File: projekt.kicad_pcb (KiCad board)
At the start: 4 copper layers, 65 x 65 mm, 118 parts, among them IC1 DW01+G, IC4 MIC5504-3.3YM5-TR, J1 10118194-0001LF, J10 Conn_01x06_Pin, J2 TP4056, J4 Conn_01x02_Socket, Q1 AO3420, Q2 AO3420, Q3 AO3420, Q4 AO3420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

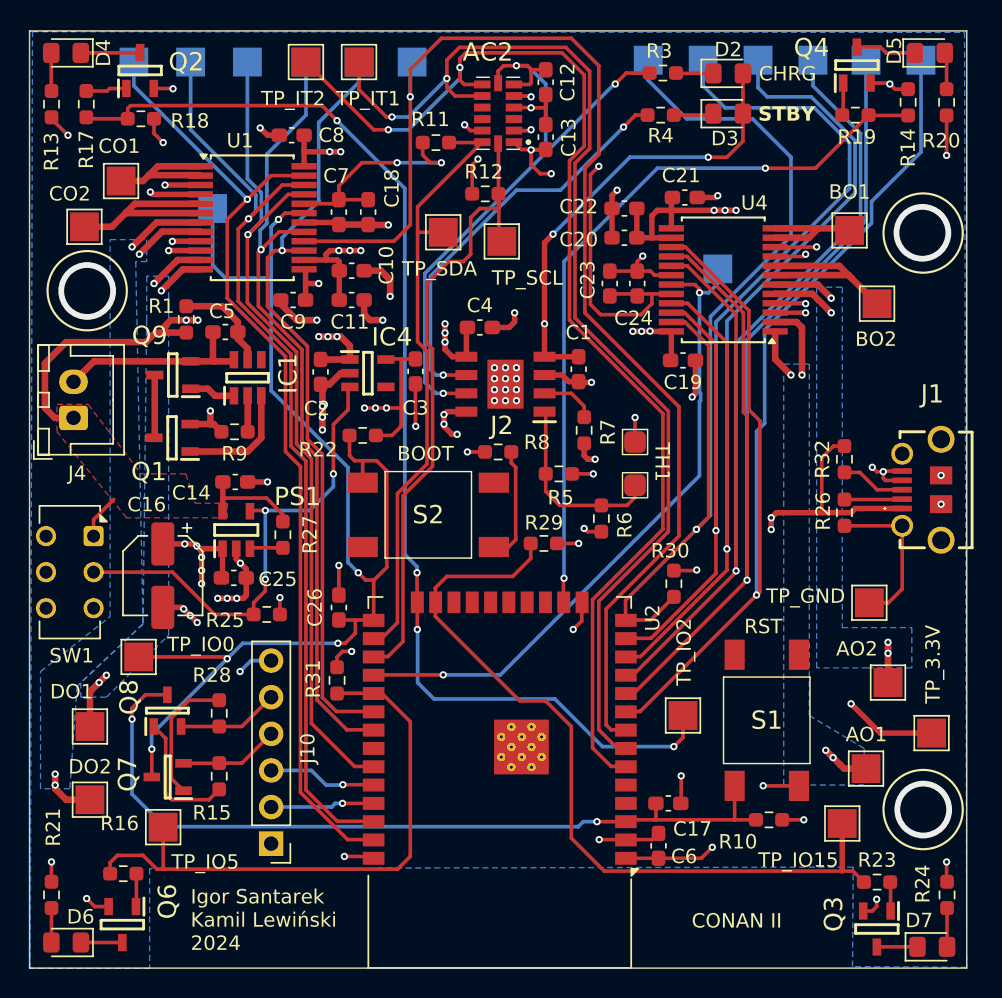
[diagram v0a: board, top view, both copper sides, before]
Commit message: Podmiana esp32 i footprinta switcha
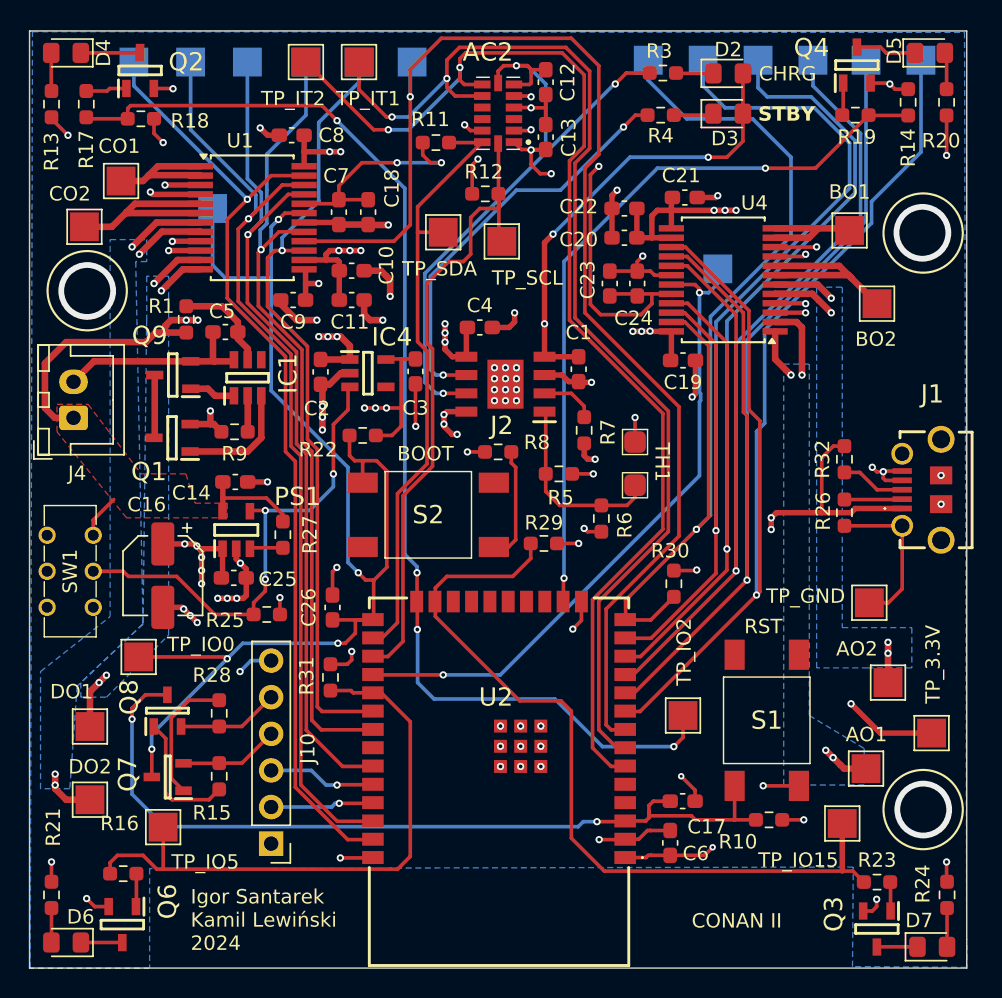
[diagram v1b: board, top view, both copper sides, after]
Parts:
- SW1: footprint Button_Switch_THT:SW_CK_JS202011AQN_DPDT_Angled -> Button_Switch_THT:SS22T20
- U2: value ESP32-WROOM-32E -> ESP32-WROOM-32E-N16; footprint RF_Module:ESP32-WROOM-32D -> SamacSys_Parts:ESP32WROOM32EN16
- moved SW1 2.93 mm to (119.0, 102.4), turned to 90 degrees
- moved U2 2.69 mm to (148.8, 116.7)
- moved C17 1.00 mm to (161.5, 118.3)
- moved C6 0.83 mm to (160.6, 121.2)
- moved R31 0.50 mm to (137.1, 109.7)
- moved C26 0.44 mm to (137.2, 104.9)
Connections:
- SW1 pad 1: /LIPO+ -> unconnected-(SW1-A-Pad1)
- SW1 pad 2: /SW+ -> unconnected-(SW1-B-Pad2)
- SW1 pad 5: unconnected-(SW1-B-Pad5) -> /SW+
- SW1 pad 6: unconnected-(SW1-C-Pad6) -> /LIPO+
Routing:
- net /EN: track 56.9 -> 58.8 mm
- net /BOOT: track 85.1 -> 86.7 mm
- net +3.3V: track 84.6 -> 85.8 mm
- net /DIN1: track 55.6 -> 56.7 mm
- net /LED3: track 55.7 -> 56.3 mm
- net /PWMD: track 54.1 -> 54.6 mm
- net GND: track 138.1 -> 138.6 mm, vias 73 -> 82

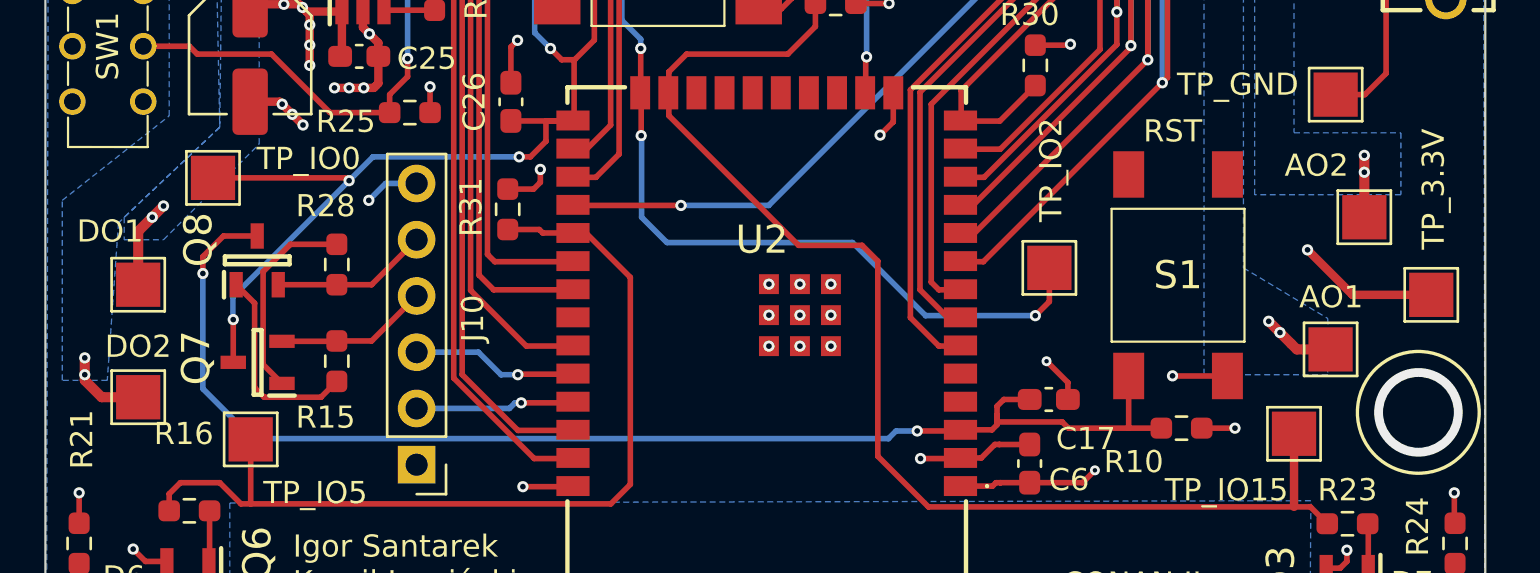
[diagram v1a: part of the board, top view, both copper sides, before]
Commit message: Podmiana ścieżek na plane w dolnych wyjściach silników
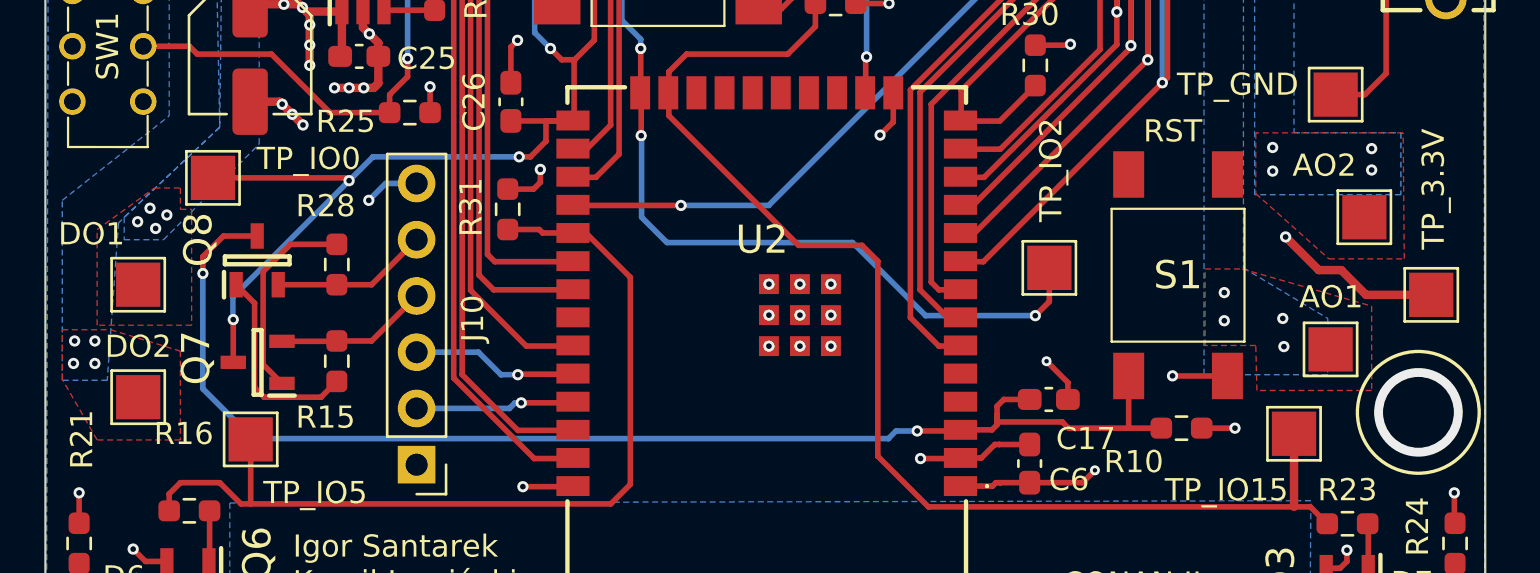
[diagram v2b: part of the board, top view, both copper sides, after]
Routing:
- net Net-(DO1-Pin_1): track 11.2 -> 7.22 mm, vias 4 -> 6
- net Net-(DO2-Pin_1): track 14.1 -> 10.3 mm, vias 4 -> 6
- net Net-(AO1-Pin_1): track 12.1 -> 8.80 mm, vias 4 -> 6
- net Net-(AO2-Pin_1): track 11.5 -> 8.73 mm, vias 4 -> 6
- net +3.3V: track 85.8 -> 87.0 mm
- added copper zone on F.Cu, net Net-(AO1-Pin_1)
- added copper zone on F.Cu, net Net-(AO2-Pin_1)
- added copper zone on F.Cu, net Net-(DO1-Pin_1)
- added copper zone on F.Cu, net Net-(DO2-Pin_1)

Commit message: Przed wygenerowaniem gerberów
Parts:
- D2: value GREEN -> RED
- D3: value RED -> GREEN
- R13, R20: value 120 -> 68
- R21, R24: value 320 -> 120
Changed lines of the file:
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@@
 			)
 		)
-		(property "Value" "320"
+		(property "Value" "120"
 			(at 0 1.43 90)
 			(layer "F.Fab")
@@
 			)
 		)
-		(property "Value" "320"
+		(property "Value" "120"
 			(at -0.018 1.524 90)
 			(layer "F.Fab")
@@
 			)
 		)
-		(property "Value" "RED"
+		(property "Value" "GREEN"
 			(at 3.5306 0.2032 0)
 			(layer "F.Fab")
@@
 			)
 		)
-		(property "Value" "GREEN"
+		(property "Value" "RED"
 			(at 0 1.65 0)
 			(layer "F.Fab")
@@
 			)
 		)
-		(property "Value" "120"
+		(property "Value" "68"
 			(at 0 1.43 90)
 			(layer "F.Fab")
@@
 			)
 		)
-		(property "Value" "120"
+		(property "Value" "68"
 			(at 0 1.43 90)
 			(layer "F.Fab")

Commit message: Przed wygenerowaniem gerberów
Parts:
- added G***: LOGO, Graphics:acc_dir_img, F.Cu at (151.8, 77.0)
- moved DO1 0.35 mm to (120.5, 112.8)

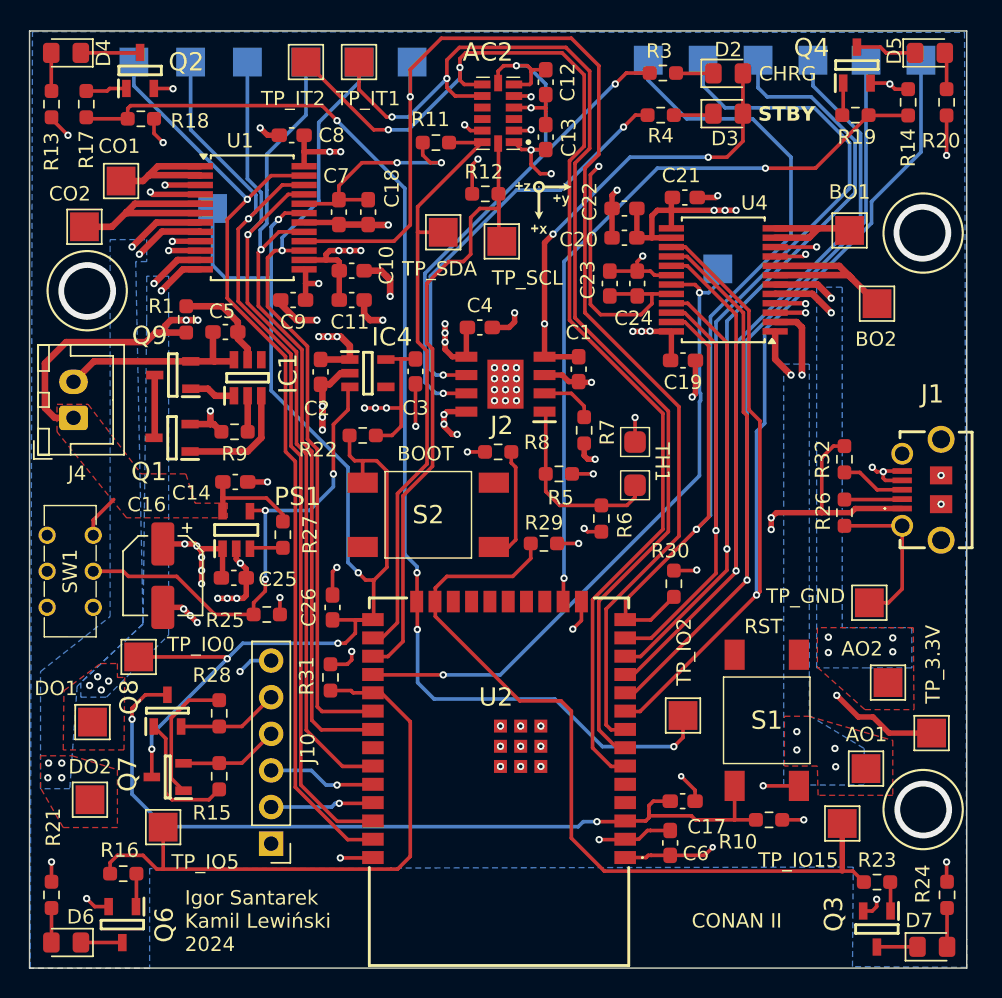
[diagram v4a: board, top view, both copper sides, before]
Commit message: poprawienie włąściwości odprowadzania ciepła dla power switcha
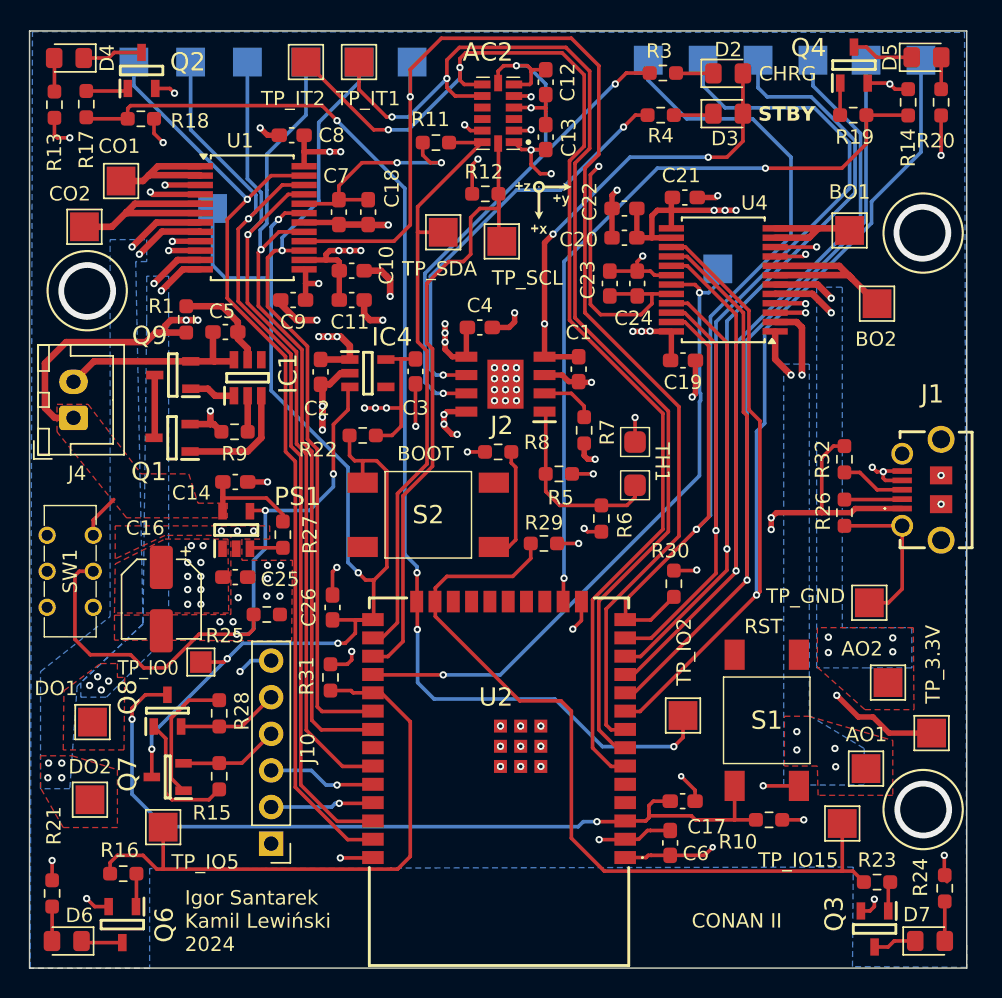
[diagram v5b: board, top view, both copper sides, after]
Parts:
- TP4: footprint TestPoint:TestPoint_Pad_2.0x2.0mm -> TestPoint:TestPoint_Pad_1.5x1.5mm
- moved TP4 4.33 mm to (128.1, 108.7)
- moved C16 1.63 mm to (125.3, 104.3)
- moved R24 0.48 mm to (179.7, 124.4)
- moved D7 0.44 mm to (178.7, 128.0)
- moved D4 0.41 mm to (118.9, 66.8)
- moved D5 0.39 mm to (178.4, 66.7)
- moved R20 0.38 mm to (179.4, 69.8)
- moved R13 0.21 mm to (117.9, 70.0)
- moved Q4 0.20 mm to (173.4, 67.2)
- moved Q3 0.16 mm to (174.8, 127.2)
- moved R19 0.15 mm to (173.3, 70.7)
- moved C25 0.11 mm to (130.5, 102.8)
- moved R21 0.11 mm to (117.7, 124.7)
- moved D6 0.11 mm to (118.8, 128.0)
- moved Q2 0.10 mm to (124.0, 67.6)
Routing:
- net /SW+: track 33.8 -> 44.9 mm
- net GND: track 138.6 -> 129.4 mm, vias 82 -> 85
- net /PWR+: track 50.7 -> 42.6 mm, vias 21 -> 26
- net /BOOT: track 86.7 -> 82.4 mm
- net /LED4: track 51.7 -> 52.9 mm
- added copper zone on F.Cu, net /PWR+
- added copper zone on F.Cu, net GND

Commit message: poprawienie przelotek
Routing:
- net GND: track 129.4 -> 130.6 mm

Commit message: Wysłane do produkcji
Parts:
- moved TP24 24.4 mm to (174.9, 89.5)
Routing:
- net +3.3V: track 87.0 -> 82.0 mm
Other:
- board text added: "TP_3.3V"
- board text added: "TP_AIN1"
- board text added: "TP_AIN2"
- board text added: "TP_BIN1"
- board text added: "TP_BIN2"
- board text added: "TP_CIN1"
- board text added: "TP_CIN2"
- board text added: "TP_DIN1"
- board text added: "TP_DIN2"
- board text added: "TP_GND"
- board text added: "TP_IO0"
- board text added: "TP_IO15"
- board text added: "TP_IO2"
- board text added: "TP_IO5"
- board text added: "TP_IT1"
- board text added: "TP_IT2"
- board text added: "TP_PWMA_IO12"
- board text added: "TP_PWMB"
- board text added: "TP_PWMC"
- board text added: "TP_PWMD"
- board text added: "TP_SCL"
- board text added: "TP_SDA"
- board text added: "TP_STBY1"
- board text added: "TP_STBY2"
